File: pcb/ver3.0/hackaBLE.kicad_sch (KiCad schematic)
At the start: 32 parts, among them J1 GPIO, J2 GPIO, J3 GPIO, J5 GPIO, J7 SWD, SW1 SW_Push, U1 nrf52832, U3 RF_Antenna, Y1 32.768KHz, Y2 32MHz

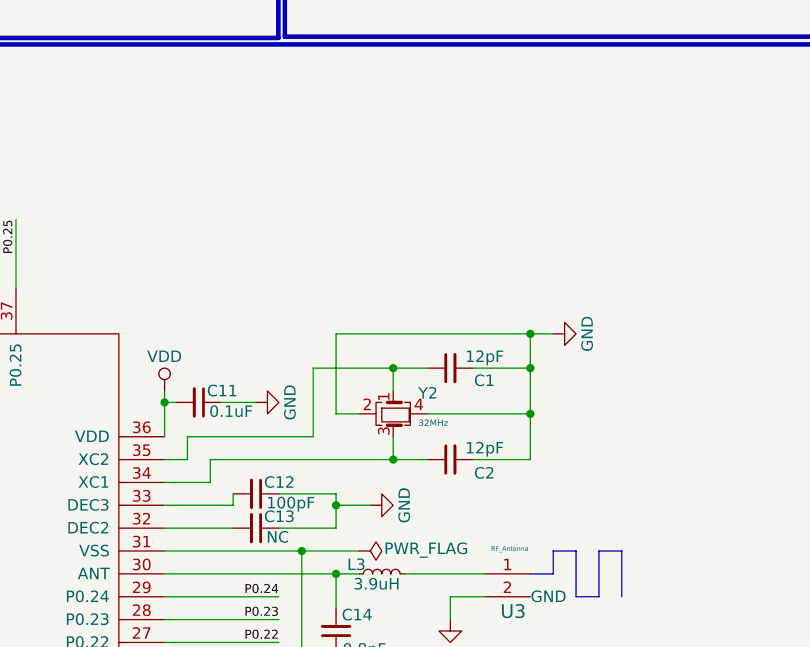
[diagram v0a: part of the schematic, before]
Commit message: now Version 3.0 has no Error and ready for manufacturing.
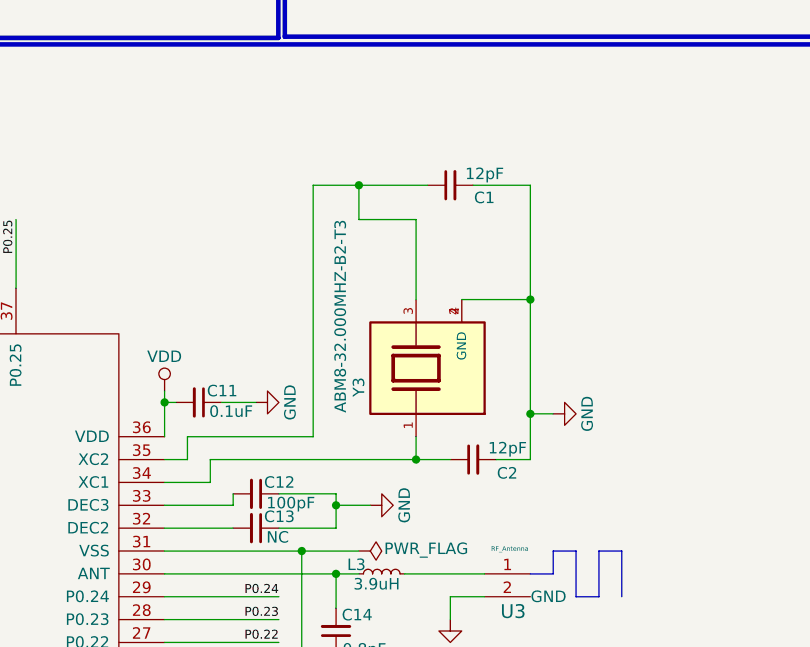
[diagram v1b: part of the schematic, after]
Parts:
- removed Y2: 32MHz, hackaBLE:32MHz_crystal, symbol hackaBLE-rescue:Crystal_GND24_Small
- added Y3: ABM8-32.000MHZ-B2-T3, crystal:XTAL_ABM8-32.000MHZ-B2-T3, symbol SparkFun-Clock:ABM8-32.000MHZ-B2-T3
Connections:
- net GND: now also Y3.2 (GND), Y3.4 (GND)
- net at C2.1, U1.34 (XC1): now also Y3.1
- net at C1.1, U1.35 (XC2): now also Y3.3
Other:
- moved on the sheet: C1, C2
